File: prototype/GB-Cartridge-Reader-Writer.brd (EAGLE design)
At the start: 100 x 80 mm, 37 parts, among them IC1 74HC595N, IC2 74HC595N

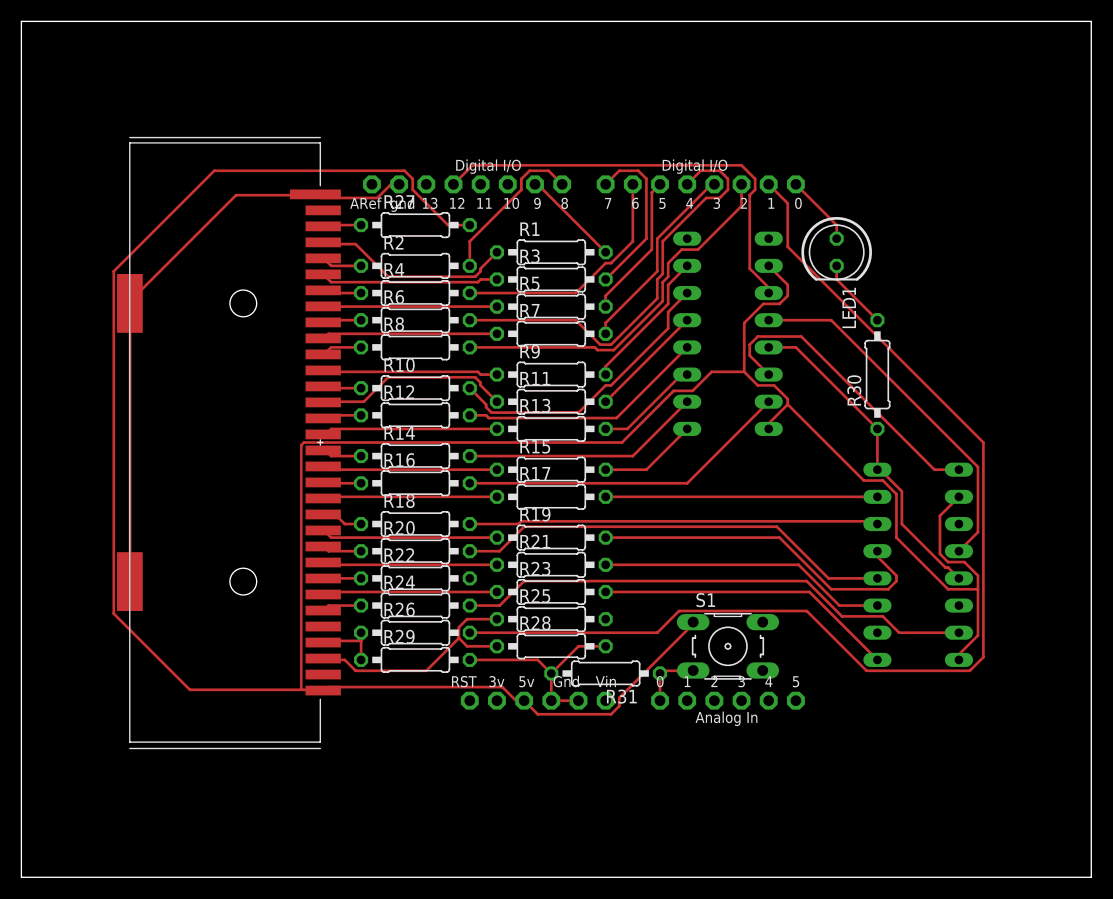
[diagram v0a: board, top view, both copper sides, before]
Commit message: moved some components - no functionial changes
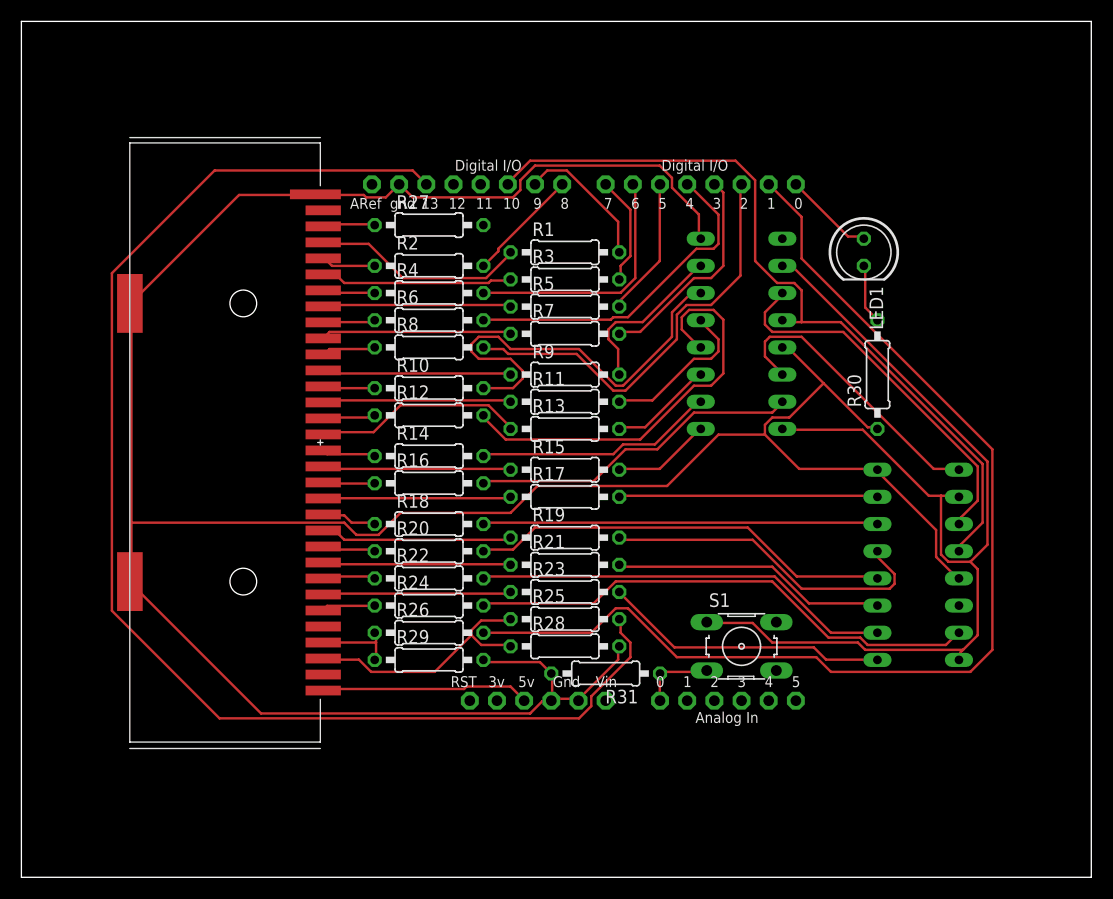
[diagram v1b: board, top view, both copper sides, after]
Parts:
- moved LED1 2.54 mm to (78.7, 58.4)
- moved R10 1.27 mm to (38.1, 45.7)
- moved R12 1.27 mm to (38.1, 43.2)
- moved R14 1.27 mm to (38.1, 39.4)
- moved R16 1.27 mm to (38.1, 36.8)
- moved R18 1.27 mm to (38.1, 33.0)
- moved R2 1.27 mm to (38.1, 57.1)
- moved R20 1.27 mm to (38.1, 30.5)
- moved R22 1.27 mm to (38.1, 27.9)
- moved R24 1.27 mm to (38.1, 25.4)
- moved R26 1.27 mm to (38.1, 22.9)
- moved R27 1.27 mm to (38.1, 61.0)
- moved R29 1.27 mm to (38.1, 20.3)
- moved R4 1.27 mm to (38.1, 54.6)
- moved R6 1.27 mm to (38.1, 52.1)
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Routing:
- net N$62: track 106.4 -> 264.0 mm
- net N$51: track 269.7 -> 119.2 mm
- net N$54: track 0.00 -> 125.0 mm
- net N$59: track 33.8 -> 74.2 mm
- net N$30: track 0.00 -> 39.2 mm
- net N$37: track 23.2 -> 39.2 mm
- net N$60: track 26.9 -> 39.5 mm
- net N$52: track 39.6 -> 31.8 mm
- net N$42: track 41.1 -> 35.1 mm
- net N$56: track 15.6 -> 10.3 mm
- net N$48: track 34.9 -> 40.1 mm
- net N$57: track 14.8 -> 10.7 mm
- net N$41: track 9.23 -> 13.3 mm
- net N$38: track 10.8 -> 14.8 mm
- net N$13: track 16.5 -> 19.7 mm
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
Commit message: made traces wider; wired wire bridges on bottom layer to get the vias for drilling; more space between traces;
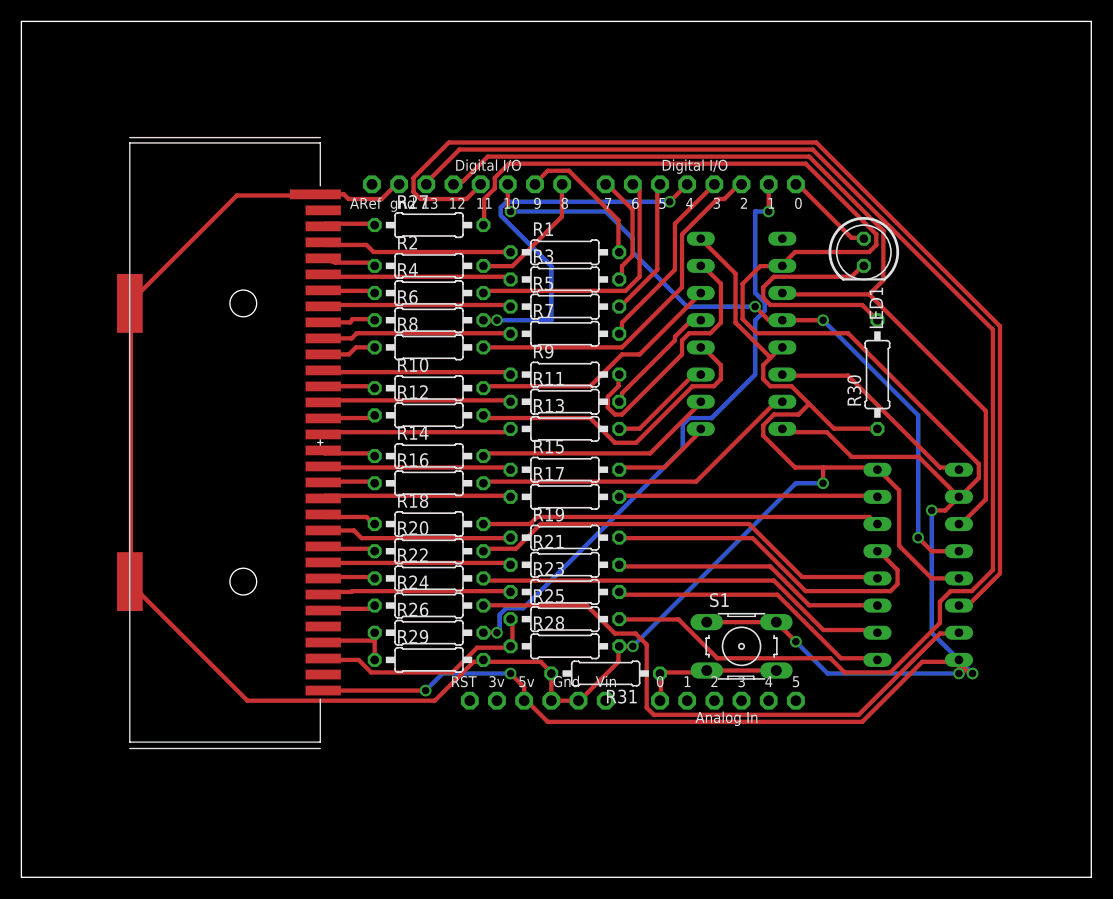
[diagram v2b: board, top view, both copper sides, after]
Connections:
- net N$51: now also S1.2
- net N$65: now also S1.4
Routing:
- net N$51: track 119.2 -> 226.2 mm, vias 0 -> 6
- net N$61: track 0.00 -> 99.9 mm
- net N$62: track 264.0 -> 205.1 mm, vias 0 -> 2
- net N$42: track 35.1 -> 85.9 mm
- net N$46: track 104.0 -> 57.4 mm, vias 0 -> 2
- net N$58: track 5.68 -> 22.7 mm
- net N$60: track 39.5 -> 24.1 mm
- net N$37: track 39.2 -> 29.7 mm
- net N$40: track 15.7 -> 24.9 mm
- net N$59: track 74.2 -> 65.1 mm, vias 0 -> 4
- net N$49: track 27.2 -> 20.2 mm
- net N$25: track 48.4 -> 55.3 mm
- net N$48: track 40.1 -> 33.3 mm
- net N$65: track 7.05 -> 13.7 mm
- net N$52: track 31.8 -> 37.2 mm, vias 0 -> 2
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
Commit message: moved one ic due to space issues
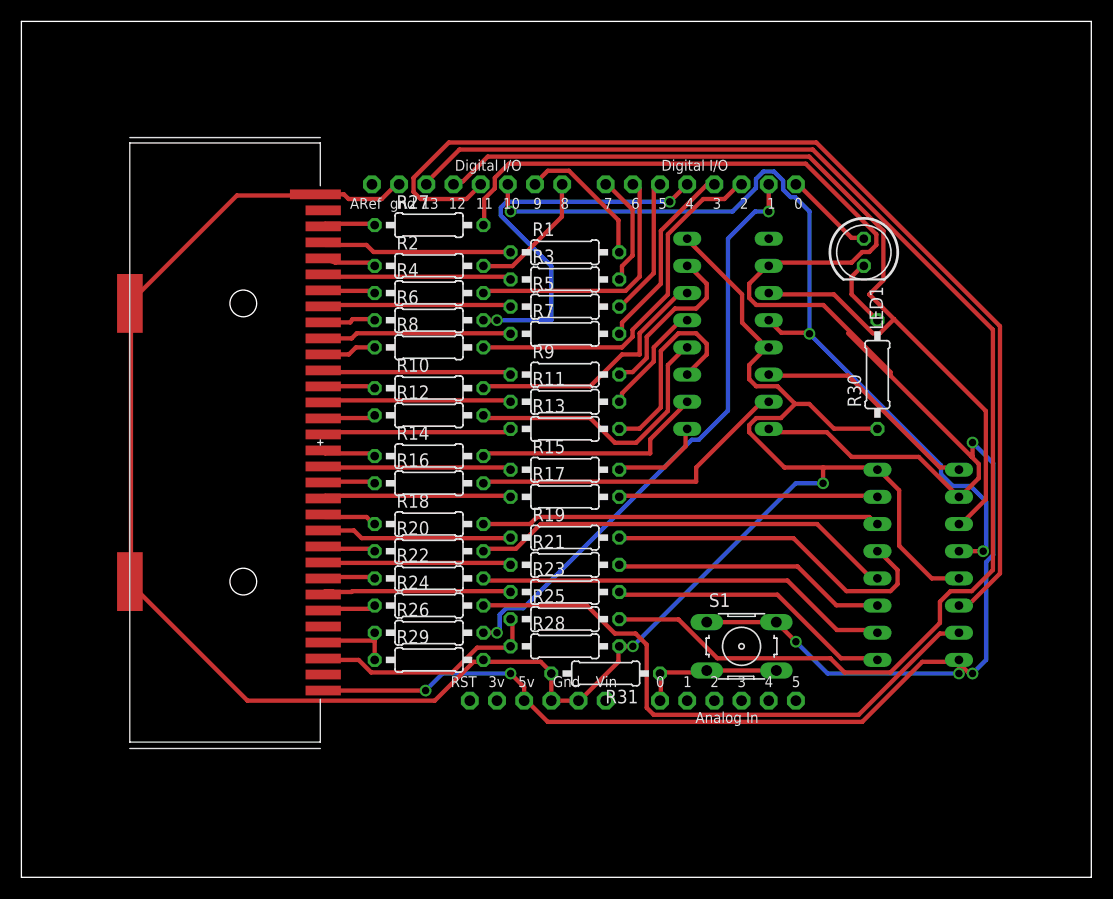
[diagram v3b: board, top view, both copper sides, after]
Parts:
- moved IC1 1.27 mm to (66.0, 50.8)
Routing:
- net N$58: track 22.7 -> 6.62 mm
- net N$59: track 65.1 -> 81.1 mm, vias 4 -> 3
- net N$51: track 226.2 -> 235.6 mm
- net N$39: track 9.71 -> 19.0 mm
- net N$40: track 24.9 -> 16.3 mm
- net N$42: track 85.9 -> 91.6 mm
- net N$37: track 29.7 -> 26.4 mm
- net N$46: track 57.4 -> 55.8 mm
- net N$62: track 205.1 -> 206.5 mm
- net N$49: track 20.2 -> 21.5 mm
- net N$23: track 16.6 -> 17.8 mm
- net N$48: track 33.3 -> 34.1 mm
- net N$38: track 11.4 -> 10.7 mm
- net N$34: track 9.28 -> 8.75 mm
- net N$35: track 22.5 -> 22.0 mm
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
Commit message: license, layout improvements, png, submodules, readme
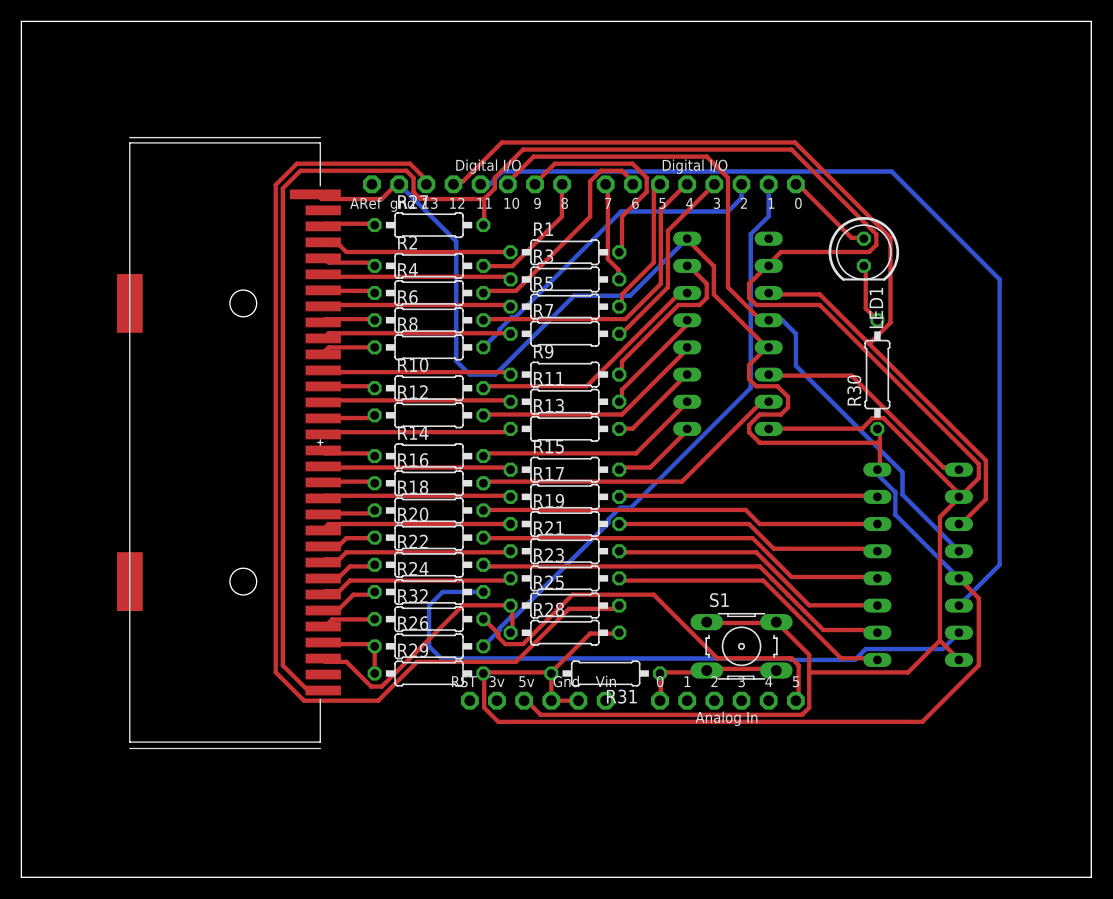
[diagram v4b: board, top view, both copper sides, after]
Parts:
- added R32: 470R, rcl:0207/10
- moved R19 1.27 mm to (50.8, 33.0)
- moved R24 1.27 mm to (38.1, 26.7)
- moved R20 1.27 mm to (38.1, 31.8)
- moved R21 1.27 mm to (50.8, 30.5)
- moved R22 1.27 mm to (38.1, 29.2)
- moved R23 1.27 mm to (50.8, 27.9)
- moved R25 1.27 mm to (50.8, 25.4)
- moved R26 1.27 mm to (38.1, 21.6)
- moved R28 1.27 mm to (50.8, 22.9)
- moved R29 1.27 mm to (38.1, 19.1)
- moved R18 1.27 mm to (38.1, 34.3)
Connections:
- new net N$27: R32.1, U$2.5
- new net N$64: R32.2, U$1.A5
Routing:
- net N$64: track 0.00 -> 38.8 mm
- net N$54: track 125.9 -> 98.6 mm
- net N$51: track 235.6 -> 258.0 mm, vias 6 -> 0
- net N$61: track 99.9 -> 85.2 mm
- net N$59: track 81.1 -> 67.6 mm, vias 3 -> 0
- net N$62: track 206.5 -> 193.0 mm, vias 2 -> 0
- net N$39: track 19.0 -> 8.43 mm
- net N$52: track 37.2 -> 28.4 mm, vias 2 -> 0
- net N$33: track 32.2 -> 25.2 mm
- net N$41: track 13.3 -> 20.0 mm
- net N$25: track 55.3 -> 60.5 mm
- net N$27: track 0.00 -> 5.11 mm
- net N$37: track 26.4 -> 22.0 mm
- net N$55: track 24.3 -> 21.4 mm
- net N$48: track 34.1 -> 31.3 mm
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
